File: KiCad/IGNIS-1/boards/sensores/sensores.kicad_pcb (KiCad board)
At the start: 2 copper layers, 10 parts, among them J41 Backplane_2x10, U20 BME280, U21 MPU6050, U22 MQ-135, U24 GPS NEO-6M

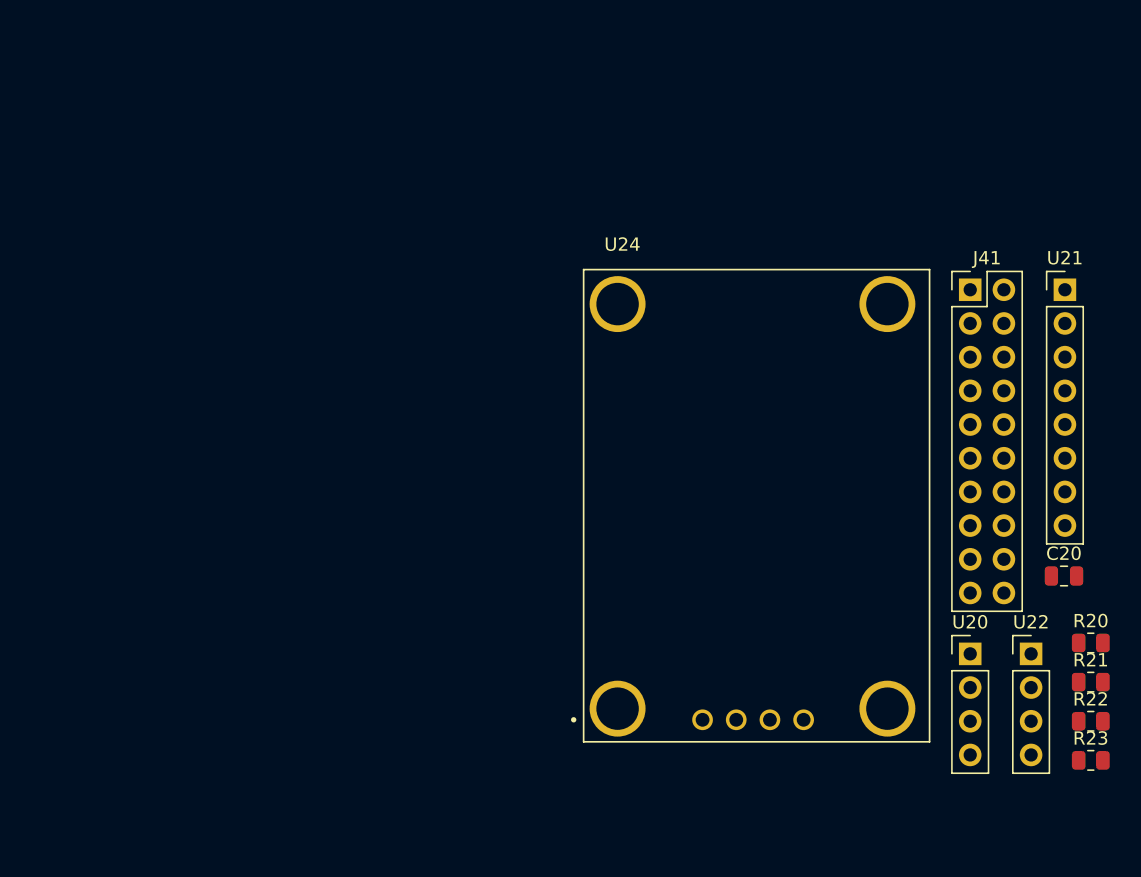
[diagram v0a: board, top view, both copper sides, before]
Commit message: Actualizado los boards de IGNIS - separado en 3 boards
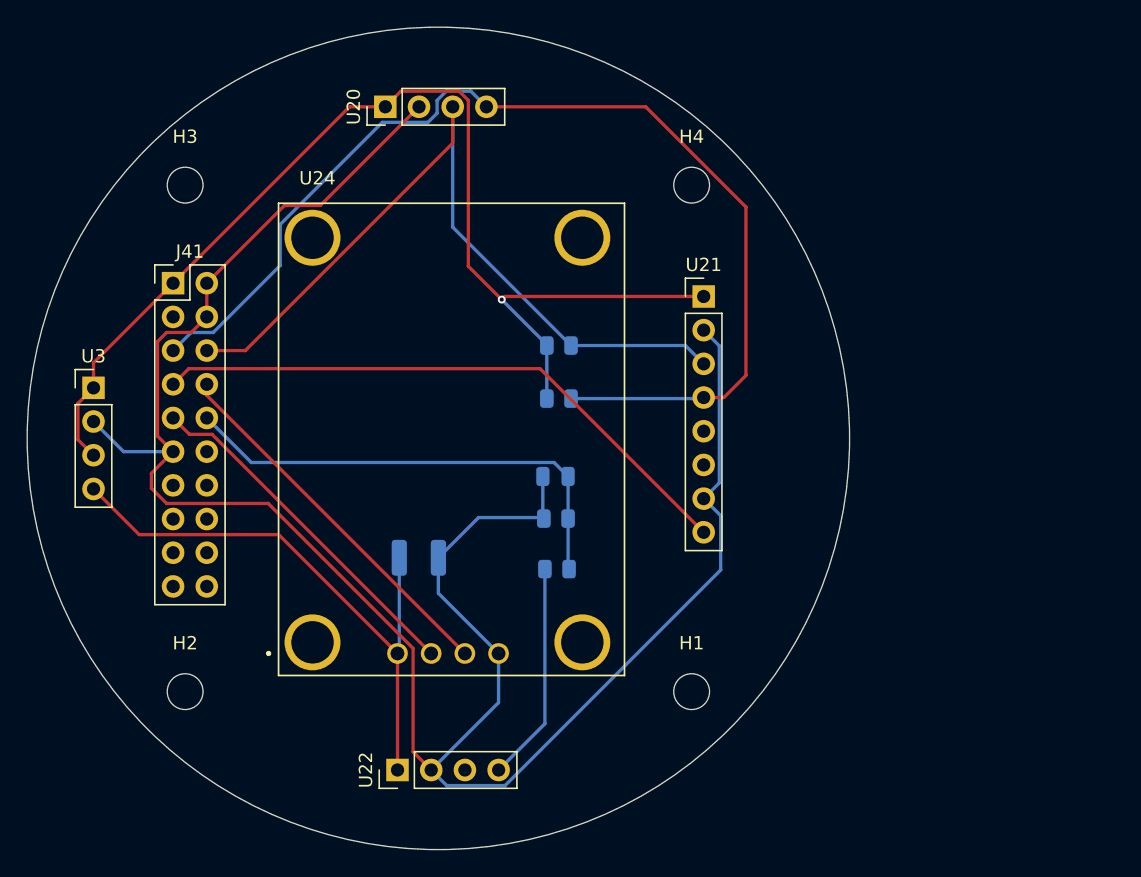
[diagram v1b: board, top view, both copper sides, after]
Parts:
- added C4: 220uF, Capacitor_SMD:C_1210_3225Metric, B.Cu at (98.5, 109.0)
- added H1: M2.5_hole, MountingHole:MountingHole_2.7mm_M2.5, F.Cu at (119.1, 119.1)
- added H2: M2.5_hole, MountingHole:MountingHole_2.7mm_M2.5, F.Cu at (80.9, 119.1)
- added H3: M2.5_hole, MountingHole:MountingHole_2.7mm_M2.5, F.Cu at (80.9, 80.9)
- added H4: M2.5_hole, MountingHole:MountingHole_2.7mm_M2.5, F.Cu at (119.1, 80.9)
- added U3: Boost_5V, Connector_PinHeader_2.54mm:PinHeader_1x04_P2.54mm_Vertical, F.Cu at (74.0, 96.2)
- C20, R20, R21, R22, R23: moved to B.Cu
- moved U20 60.4 mm to (96.0, 75.0), turned to 90 degrees
- moved J41 60.1 mm to (80.0, 88.3)
- moved U22 48.6 mm to (96.9, 125.0), turned to 90 degrees
- moved R21 47.5 mm to (109.1, 93.0), turned to 180 degrees
- moved R23 44.3 mm to (108.9, 106.0), turned to 180 degrees
- moved R20 44.1 mm to (109.1, 97.0), turned to 180 degrees
- moved R22 41.8 mm to (108.9, 109.9)
- moved C20 39.1 mm to (108.8, 102.9), turned to 180 degrees
- moved U21 27.2 mm to (120.0, 89.3)
- moved U24 23.5 mm to (101.1, 100.1)
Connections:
- J41 pad 3: +5V -> unconnected-(J41-Pin_3-Pad3)
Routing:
- net GND: track 0.00 -> 163.1 mm
- net +3V3: track 0.00 -> 85.2 mm, vias 0 -> 1
- net SDA: track 0.00 -> 83.9 mm
- net SCL: track 0.00 -> 60.0 mm
- net MPU_INT: track 0.00 -> 45.6 mm
- net +5V: track 0.00 -> 44.1 mm
- net MQ_AOUT: track 0.00 -> 36.1 mm
- net GPS_TX: track 0.00 -> 28.4 mm
- net GPS_RX: track 0.00 -> 26.8 mm
- net /MQ_A0_RAW: track 0.00 -> 16.6 mm
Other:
- board outline added: 62 x 62 mm
